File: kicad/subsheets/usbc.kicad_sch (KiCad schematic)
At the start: 15 parts

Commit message: Mark as R1.0
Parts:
- renumbered C5 to C6, C6 to C7, FB1 to FB2, FB2 to FB3, R46 to R17, R52 to R18
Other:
- company: (none) -> UVic Rocketry
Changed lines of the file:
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@@
 	(title_block
 		(title "USB C Port")
+		(date "2025-11-23")
+		(rev "1.0")
+		(company "UVic Rocketry")
+		(comment 1 "Author: Eric Handley")
 	)
 	(junction
@@
 		(on_board yes)
 		(dnp no)
-		(property "Reference" "#PWR093"
+		(property "Reference" "#PWR028"
 			(at 161.29 132.08 0)
 			(effects
@@
 			(project "srad-camera"
 				(path "/da62c771-e8c9-451f-8df1-ec995aadcb11/2d2335c5-b8ff-4d43-ae83-f45f6f125b07"
-					(reference "#PWR093")
+					(reference "#PWR028")
 					(unit 1)
 				)
@@
 		(on_board yes)
 		(dnp no)
-		(property "Reference" "FB1"
+		(property "Reference" "FB2"
 			(at 169.926 68.072 90)
 			(effects
@@
 			(project "srad-camera"
 				(path "/da62c771-e8c9-451f-8df1-ec995aadcb11/2d2335c5-b8ff-4d43-ae83-f45f6f125b07"
-					(reference "FB1")
+					(reference "FB2")
 					(unit 1)
 				)
@@
 		(on_board yes)
 		(dnp no)
-		(property "Reference" "#PWR019"
+		(property "Reference" "#PWR024"
 			(at 176.53 86.36 0)
 			(effects
@@
 			(project "srad-camera"
 				(path "/da62c771-e8c9-451f-8df1-ec995aadcb11/2d2335c5-b8ff-4d43-ae83-f45f6f125b07"
-					(reference "#PWR019")
+					(reference "#PWR024")
 					(unit 1)
 				)
@@
 		(dnp no)
 		(fields_autoplaced yes)
-		(property "Reference" "#PWR092"
+		(property "Reference" "#PWR026"
 			(at 156.21 116.84 0)
 			(effects
@@
 			(project "srad-camera"
 				(path "/da62c771-e8c9-451f-8df1-ec995aadcb11/2d2335c5-b8ff-4d43-ae83-f45f6f125b07"
-					(reference "#PWR092")
+					(reference "#PWR026")
 					(unit 1)
 				)
@@
 		(dnp no)
 		(fields_autoplaced yes)
-		(property "Reference" "C6"
+		(property "Reference" "C7"
 			(at 182.6641 72.4414 0)
 			(effects
@@
 			(project "srad-camera"
 				(path "/da62c771-e8c9-451f-8df1-ec995aadcb11/2d2335c5-b8ff-4d43-ae83-f45f6f125b07"
-					(reference "C6")
+					(reference "C7")
 					(unit 1)
 				)
@@
 		(on_board yes)
 		(dnp no)
-		(property "Reference" "FB2"
+		(property "Reference" "FB3"
 			(at 118.618 115.062 0)
 			(effects
@@
 			(project "srad-camera"
 				(path "/da62c771-e8c9-451f-8df1-ec995aadcb11/2d2335c5-b8ff-4d43-ae83-f45f6f125b07"
-					(reference "FB2")
+					(reference "FB3")
 					(unit 1)
 				)
@@
 		(dnp no)
 		(fields_autoplaced yes)
-		(property "Reference" "#PWR091"
+		(property "Reference" "#PWR021"
 			(at 167.64 64.77 0)
 			(effects
@@
 			(project "srad-camera"
 				(path "/da62c771-e8c9-451f-8df1-ec995aadcb11/2d2335c5-b8ff-4d43-ae83-f45f6f125b07"
-					(reference "#PWR091")
+					(reference "#PWR021")
 					(unit 1)
 				)
@@
 		(on_board yes)
 		(dnp no)
-		(property "Reference" "R52"
+		(property "Reference" "R18"
 			(at 162.56 121.158 0)
 			(effects
@@
 			(project "srad-camera"
 				(path "/da62c771-e8c9-451f-8df1-ec995aadcb11/2d2335c5-b8ff-4d43-ae83-f45f6f125b07"
-					(reference "R52")
+					(reference "R18")
 					(unit 1)
 				)
@@
 		(dnp no)
 		(fields_autoplaced yes)
-		(property "Reference" "C5"
+		(property "Reference" "C6"
 			(at 174.2059 72.4414 0)
 			(effects
@@
 			(project "srad-camera"
 				(path "/da62c771-e8c9-451f-8df1-ec995aadcb11/2d2335c5-b8ff-4d43-ae83-f45f6f125b07"
-					(reference "C5")
+					(reference "C6")
 					(unit 1)
 				)
@@
 		(dnp no)
 		(fields_autoplaced yes)
-		(property "Reference" "#PWR090"
+		(property "Reference" "#PWR022"
 			(at 134.62 73.66 0)
 			(effects
@@
 			(project ""
 				(path "/da62c771-e8c9-451f-8df1-ec995aadcb11/2d2335c5-b8ff-4d43-ae83-f45f6f125b07"
-					(reference "#PWR090")
+					(reference "#PWR022")
 					(unit 1)
 				)
@@
 		(on_board yes)
 		(dnp no)
-		(property "Reference" "#PWR020"
+		(property "Reference" "#PWR023"
 			(at 92.71 74.93 0)
 			(effects
@@
 			(project "srad-camera"
 				(path "/da62c771-e8c9-451f-8df1-ec995aadcb11/2d2335c5-b8ff-4d43-ae83-f45f6f125b07"
-					(reference "#PWR020")
+					(reference "#PWR023")
 					(unit 1)
 				)
@@
 		(on_board yes)
 		(dnp no)
-		(property "Reference" "R46"
+		(property "Reference" "R17"
 			(at 154.432 112.776 90)
 			(effects
@@
 			(project "srad-camera"
 				(path "/da62c771-e8c9-451f-8df1-ec995aadcb11/2d2335c5-b8ff-4d43-ae83-f45f6f125b07"
-					(reference "R46")
+					(reference "R17")
 					(unit 1)
 				)
@@
 		(dnp no)
 		(fields_autoplaced yes)
-		(property "Reference" "#PWR021"
+		(property "Reference" "#PWR025"
 			(at 140.97 111.76 0)
 			(effects
@@
 			(project "srad-camera"
 				(path "/da62c771-e8c9-451f-8df1-ec995aadcb11/2d2335c5-b8ff-4d43-ae83-f45f6f125b07"
-					(reference "#PWR021")
+					(reference "#PWR025")
 					(unit 1)
 				)
@@
 		(dnp no)
 		(fields_autoplaced yes)
-		(property "Reference" "#PWR022"
+		(property "Reference" "#PWR027"
 			(at 123.19 129.54 0)
 			(effects
@@
 			(project "srad-camera"
 				(path "/da62c771-e8c9-451f-8df1-ec995aadcb11/2d2335c5-b8ff-4d43-ae83-f45f6f125b07"
-					(reference "#PWR022")
+					(reference "#PWR027")
 					(unit 1)
 				)

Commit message: Start on PCB design
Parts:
- C6: footprint (none) -> Capacitor_SMD:C_0805_2012Metric; LCSC PART NAME (none) -> C15850
- C7: footprint (none) -> Capacitor_SMD:C_0402_1005Metric; LCSC PART NAME (none) -> C1525
- D2: value D_TVS <1uF -> TVS Vr3.3 Vb4; footprint (none) -> Diode_SMD:D_SOD-123F; LCSC PART NAME (none) -> C19077496
- D3: value TVS Vr3.3 Vb4 <1uF -> TVS Vr3.3 Vb4; footprint (none) -> Diode_SMD:D_SOD-123F; LCSC PART NAME (none) -> C19077496
- FB2, FB3: value FerriteBead_Small -> 120R; footprint (none) -> Resistor_SMD:R_0201_0603Metric; LCSC PART NAME (none) -> C14709
- R14: renamed from R12; footprint (none) -> Resistor_SMD:R_0402_1005Metric; LCSC PART NAME (none) -> C25905
- R15: renamed from R13; footprint (none) -> Resistor_SMD:R_0402_1005Metric; LCSC PART NAME (none) -> C25905
- R16: renamed from R14; value 2.2R -> 22R; footprint (none) -> Resistor_SMD:R_0402_1005Metric; LCSC PART NAME (none) -> C25092
- R17: renamed from R15; value 2.2R -> 22R; footprint (none) -> Resistor_SMD:R_0402_1005Metric; LCSC PART NAME (none) -> C25092
- R18: renamed from R16; footprint (none) -> Resistor_SMD:R_0402_1005Metric; LCSC PART NAME (none) -> C26083
- R19: renamed from R17; footprint (none) -> Resistor_SMD:R_0402_1005Metric; LCSC PART NAME (none) -> C25744
- R20: renamed from R18; value 15k -> 10k; footprint (none) -> Resistor_SMD:R_0402_1005Metric; LCSC PART NAME (none) -> C25744
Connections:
- net USB_DM renamed USB_DN
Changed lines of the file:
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@@
 		)
 	)
-	(hierarchical_label "USB_DM"
+	(hierarchical_label "USB_DN"
 		(shape output)
 		(at 156.21 87.63 0)
@@
 			)
 		)
-		(property "Value" "FerriteBead_Small"
+		(property "Value" "120R"
 			(at 168.148 68.58 90)
 			(effects
@@
 			)
 		)
-		(property "Footprint" ""
+		(property "Footprint" "Resistor_SMD:R_0201_0603Metric"
 			(at 171.45 66.548 90)
 			(effects
@@
 		)
 		(property "SUPPLEMENTARY FEATURES" ""
+			(at 171.45 64.77 90)
+			(effects
+				(font
+					(size 1.27 1.27)
+				)
+				(hide yes)
+			)
+		)
+		(property "LCSC PART NAME" "C14709"
 			(at 171.45 64.77 90)
 			(effects
@@
 		(dnp no)
 		(fields_autoplaced yes)
-		(property "Reference" "R14"
+		(property "Reference" "R16"
 			(at 148.59 82.9533 90)
 			(effects
@@
 			)
 		)
-		(property "Value" "2.2R"
+		(property "Value" "22R"
 			(at 148.59 85.1732 90)
 			(effects
@@
 			)
 		)
-		(property "Footprint" ""
+		(property "Footprint" "Resistor_SMD:R_0402_1005Metric"
 			(at 148.59 87.63 0)
 			(effects
@@
 		)
 		(property "SUPPLEMENTARY FEATURES" ""
+			(at 148.59 87.63 90)
+			(effects
+				(font
+					(size 1.27 1.27)
+				)
+				(hide yes)
+			)
+		)
+		(property "LCSC PART NAME" "C25092"
 			(at 148.59 87.63 90)
 			(effects
@@
 			(project "srad-camera"
 				(path "/da62c771-e8c9-451f-8df1-ec995aadcb11/2d2335c5-b8ff-4d43-ae83-f45f6f125b07"
-					(reference "R14")
+					(reference "R16")
 					(unit 1)
 				)
@@
 			)
 		)
-		(property "Footprint" ""
+		(property "Footprint" "Capacitor_SMD:C_0402_1005Metric"
 			(at 180.34 73.66 0)
 			(effects
@@
 			)
 		)
-		(property "V" ""
+		(property "LCSC PART NAME" "C1525"
 			(at 180.34 73.66 0)
 			(effects
@@
 			)
 		)
-		(property "Value" "TVS Vr3.3 Vb4 <1uF"
+		(property "Value" "TVS Vr3.3 Vb4"
 			(at 146.304 102.3621 90)
 			(effects
@@
 			)
 		)
-		(property "Footprint" ""
+		(property "Footprint" "Diode_SMD:D_SOD-123F"
 			(at 144.78 100.33 0)
 			(effects
@@
 		)
 		(property "SUPPLEMENTARY FEATURES" ""
+			(at 144.78 100.33 90)
+			(effects
+				(font
+					(size 1.27 1.27)
+				)
+				(hide yes)
+			)
+		)
+		(property "LCSC PART NAME" "C19077496"
 			(at 144.78 100.33 90)
 			(effects
@@
 			)
 		)
-		(property "Value" "FerriteBead_Small"
+		(property "Value" "120R"
 			(at 119.126 113.284 0)
 			(effects
@@
 			)
 		)
-		(property "Footprint" ""
+		(property "Footprint" "Resistor_SMD:R_0201_0603Metric"
 			(at 116.332 116.84 90)
 			(effects
@@
 		)
 		(property "SUPPLEMENTARY FEATURES" ""
+			(at 118.11 116.84 0)
+			(effects
+				(font
+					(size 1.27 1.27)
+				)
+				(hide yes)
+			)
+		)
+		(property "LCSC PART NAME" "C14709"
 			(at 118.11 116.84 0)
 			(effects
@@
 		(on_board yes)
 		(dnp no)
-		(property "Reference" "R18"
+		(property "Reference" "R20"
 			(at 162.56 121.158 0)
 			(effects
@@
 			)
 		)
-		(property "Value" "15k"
+		(property "Value" "10k"
 			(at 162.56 122.936 0)
 			(effects
@@
 			)
 		)
-		(property "Footprint" ""
+		(property "Footprint" "Resistor_SMD:R_0402_1005Metric"
 			(at 161.29 121.92 0)
 			(effects
@@
 		)
 		(property "SUPPLEMENTARY FEATURES" ""
+			(at 161.29 121.92 0)
+			(effects
+				(font
+					(size 1.27 1.27)
+				)
+				(hide yes)
+			)
+		)
+		(property "LCSC PART NAME" "C25744"
 			(at 161.29 121.92 0)
 			(effects
@@
 			(project "srad-camera"
 				(path "/da62c771-e8c9-451f-8df1-ec995aadcb11/2d2335c5-b8ff-4d43-ae83-f45f6f125b07"
-					(reference "R18")
+					(reference "R20")
 					(unit 1)
 				)
@@
 			)
 		)
-		(property "Footprint" ""
+		(property "Footprint" "Capacitor_SMD:C_0805_2012Metric"
 			(at 176.53 73.66 0)
 			(effects
@@
 		)
 		(property "SUPPLEMENTARY FEATURES" ""
+			(at 176.53 73.66 0)
+			(effects
+				(font
+					(size 1.27 1.27)
+				)
+				(hide yes)
+			)
+		)
+		(property "LCSC PART NAME" "C15850"
 			(at 176.53 73.66 0)
 			(effects
@@
 			)
 		)
-		(property "Value" "D_TVS <1uF"
+		(property "Value" "TVS Vr3.3 Vb4"
 			(at 143.51 101.5999 90)
 			(effects
@@
 			)
 		)
-		(property "Footprint" ""
+		(property "Footprint" "Diode_SMD:D_SOD-123F"
 			(at 140.97 100.33 0)
 			(effects
@@
 		)
 		(property "SUPPLEMENTARY FEATURES" ""
+			(at 140.97 100.33 90)
+			(effects
+				(font
+					(size 1.27 1.27)
+				)
+				(hide yes)
+			)
+		)
+		(property "LCSC PART NAME" "C19077496"
 			(at 140.97 100.33 90)
 			(effects
@@
 		(dnp no)
 		(fields_autoplaced yes)
-		(property "Reference" "R12"
+		(property "Reference" "R14"
 			(at 104.14 68.9833 90)
 			(effects
@@
 			)
 		)
-		(property "Footprint" ""
+		(property "Footprint" "Resistor_SMD:R_0402_1005Metric"
 			(at 104.14 73.66 0)
 			(effects
@@
 		)
 		(property "SUPPLEMENTARY FEATURES" ""
+			(at 104.14 73.66 90)
+			(effects
+				(font
+					(size 1.27 1.27)
+				)
+				(hide yes)
+			)
+		)
+		(property "LCSC PART NAME" "C25905"
 			(at 104.14 73.66 90)
 			(effects
@@
 			(project "srad-camera"
 				(path "/da62c771-e8c9-451f-8df1-ec995aadcb11/2d2335c5-b8ff-4d43-ae83-f45f6f125b07"
-					(reference "R12")
+					(reference "R14")
 					(unit 1)
 				)
@@
 		(on_board yes)
 		(dnp no)
-		(property "Reference" "R17"
+		(property "Reference" "R19"
 			(at 154.432 112.776 90)
 			(effects
@@
 			)
 		)
-		(property "Footprint" ""
+		(property "Footprint" "Resistor_SMD:R_0402_1005Metric"
 			(at 156.21 116.84 0)
 			(effects
@@
 		(property "SUPPLEMENTARY FEATURES" ""
 			(at 156.21 116.84 0)
+			(effects
+				(font
+					(size 1.27 1.27)
+				)
+				(hide yes)
+			)
+		)
+		(property "LCSC PART NAME" "C25744"
+			(at 156.21 116.84 90)
 			(effects
 				(font
@@
 			(project "srad-camera"
 				(path "/da62c771-e8c9-451f-8df1-ec995aadcb11/2d2335c5-b8ff-4d43-ae83-f45f6f125b07"
-					(reference "R17")
+					(reference "R19")
 					(unit 1)
 				)
@@
 		(on_board yes)
 		(dnp no)
-		(property "Reference" "R16"
+		(property "Reference" "R18"
 			(at 111.252 116.078 0)
 			(effects
@@
 			)
 		)
-		(property "Footprint" ""
+		(property "Footprint" "Resistor_SMD:R_0402_1005Metric"
 			(at 113.03 116.84 0)
 			(effects
@@
 		)
 		(property "SUPPLEMENTARY FEATURES" ""
+			(at 113.03 116.84 0)
+			(effects
+				(font
+					(size 1.27 1.27)
+				)
+				(hide yes)
+			)
+		)
+		(property "LCSC PART NAME" "C26083"
 			(at 113.03 116.84 0)
 			(effects
@@
 			(project "srad-camera"
 				(path "/da62c771-e8c9-451f-8df1-ec995aadcb11/2d2335c5-b8ff-4d43-ae83-f45f6f125b07"
-					(reference "R16")
+					(reference "R18")
 					(unit 1)
 				)
@@
 		(dnp no)
 		(fields_autoplaced yes)
-		(property "Reference" "R15"
+		(property "Reference" "R17"
 			(at 148.59 94.9623 90)
 			(effects
@@
 			)
 		)
-		(property "Value" "2.2R"
+		(property "Value" "22R"
 			(at 148.59 97.1822 90)
 			(effects
@@
 			)
 		)
-		(property "Footprint" ""
+		(property "Footprint" "Resistor_SMD:R_0402_1005Metric"
 			(at 148.59 92.71 0)
 			(effects
@@
 		)
 		(property "SUPPLEMENTARY FEATURES" ""
+			(at 148.59 92.71 90)
+			(effects
+				(font
+					(size 1.27 1.27)
+				)
+				(hide yes)
+			)
+		)
+		(property "LCSC PART NAME" "C25092"
 			(at 148.59 92.71 90)
 			(effects
@@
 			(project "srad-camera"
 				(path "/da62c771-e8c9-451f-8df1-ec995aadcb11/2d2335c5-b8ff-4d43-ae83-f45f6f125b07"
-					(reference "R15")
+					(reference "R17")
 					(unit 1)
 				)
@@
 		(dnp no)
 		(fields_autoplaced yes)
-		(property "Reference" "R13"
+		(property "Reference" "R15"
 			(at 104.14 78.4523 90)
 			(effects
@@
 			)
 		)
-		(property "Footprint" ""
+		(property "Footprint" "Resistor_SMD:R_0402_1005Metric"
 			(at 104.14 76.2 0)
 			(effects
@@
 		)
 		(property "SUPPLEMENTARY FEATURES" ""
+			(at 104.14 76.2 90)
+			(effects
+				(font
+					(size 1.27 1.27)
+				)
+				(hide yes)
+			)
+		)
+		(property "LCSC PART NAME" "C25905"
 			(at 104.14 76.2 90)
 			(effects
@@
 			(project "srad-camera"
 				(path "/da62c771-e8c9-451f-8df1-ec995aadcb11/2d2335c5-b8ff-4d43-ae83-f45f6f125b07"
-					(reference "R13")
+					(reference "R15")
 					(unit 1)
 				)

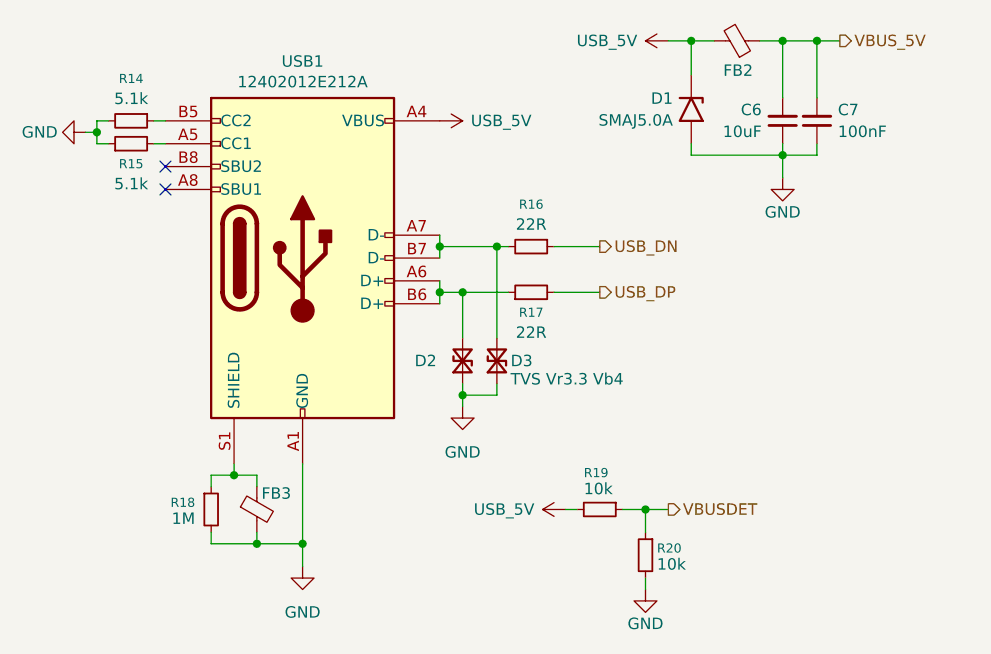
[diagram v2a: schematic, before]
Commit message: Remove power/decoupling for unused power domains
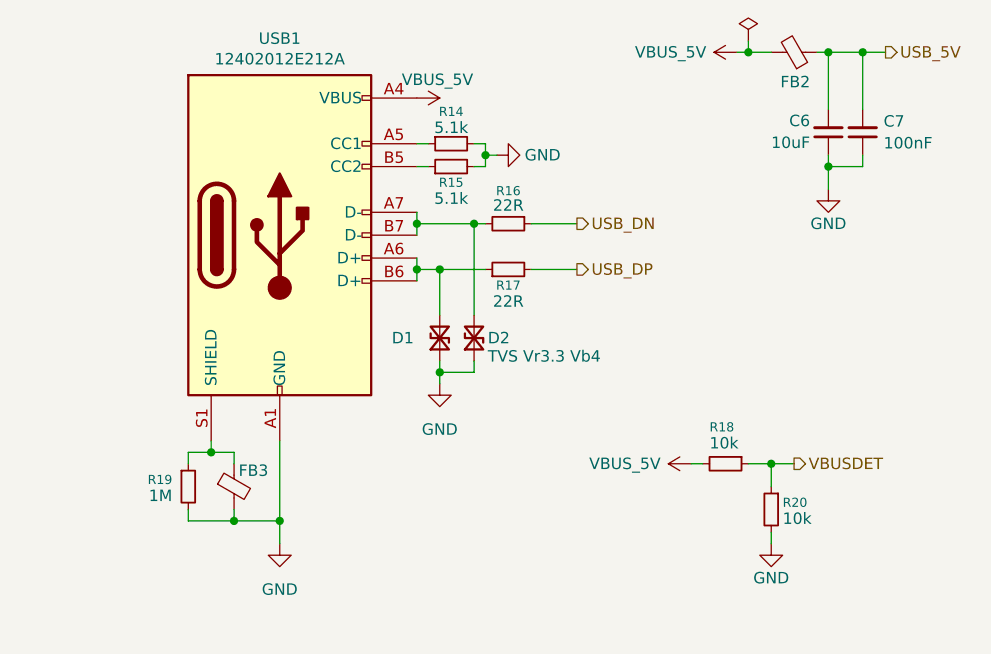
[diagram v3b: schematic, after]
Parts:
- removed D1: SMAJ5.0A, Diode_SMD:D_SMA, symbol Diode:SMAJ5.0A
- USB1: footprint srad-camera-footprints:USB-SMD_TYPE-C16PIN-1 -> Connector_USB:USB_C_Receptacle_G-Switch_GT-USB-7010ASV; symbol Connector:USB_C_Receptacle_USB2.0_16P -> Connector:USB_C_Receptacle_USB2.0_14P
- renumbered D2 to D1, D3 to D2, R19 to R18, R18 to R19
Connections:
- net GND: now also R15.2; no longer R15.1
- net USB_5V: now also C6.2, C7.2, FB2.1; no longer FB2.2, R18.2, USB1.A4 (VBUS), USB1.A9 (VBUS), USB1.B4 (VBUS), USB1.B9 (VBUS)
- net VBUS_5V: now also FB2.2, R18.2, USB1.A4 (VBUS), USB1.A9 (VBUS), USB1.B4 (VBUS), USB1.B9 (VBUS); no longer C6.2, C7.2, FB2.1
- net at USB1.A5 (CC1): now also R14.1; no longer R15.2
- net at USB1.B5 (CC2): now also R15.1; no longer R14.1
- no-connect marks 2 -> 0
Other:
- moved on the sheet: C6, C7, D1, D2, FB2, FB3, R14, R16, R17, R18, R19, R20

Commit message: All major components placed on board
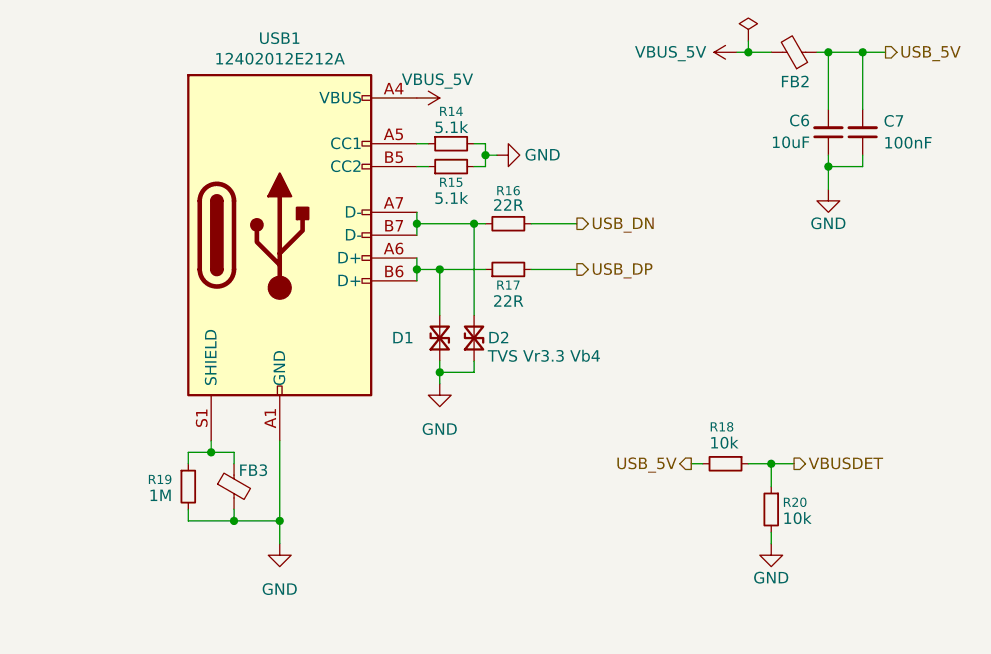
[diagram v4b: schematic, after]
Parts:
- USB1: footprint Connector_USB:USB_C_Receptacle_G-Switch_GT-USB-7010ASV -> Connector_USB:USB_C_Receptacle_HRO_TYPE-C-31-M-12
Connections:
- net USB_5V: now also R18.2
- net VBUS_5V: no longer R18.2
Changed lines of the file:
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@@
+		)
+	)
+	(hierarchical_label "USB_5V"
+		(shape output)
+		(at 166.37 111.76 180)
+		(effects
+			(font
+				(size 1.27 1.27)
+			)
+			(justify right)
 		)
 	)
@@
 				(path "/da62c771-e8c9-451f-8df1-ec995aadcb11/2d2335c5-b8ff-4d43-ae83-f45f6f125b07"
 					(reference "#PWR028")
-					(unit 1)
-				)
-			)
-		)
-	)
-	(symbol
-		(lib_id "power:VCC")
-		(at 166.37 111.76 90)
-		(unit 1)
-		(exclude_from_sim no)
-		(in_bom yes)
-		(on_board yes)
-		(dnp no)
-		(fields_autoplaced yes)
-		(property "Reference" "#PWR030"
-			(at 170.18 111.76 0)
-			(effects
-				(font
-					(size 1.27 1.27)
-				)
-				(hide yes)
-			)
-		)
-		(property "Value" "VBUS_5V"
-			(at 159.0017 111.76 90)
-			(effects
-				(font
-					(size 1.27 1.27)
-				)
-			)
-		)
-		(property "Footprint" ""
-			(at 166.37 111.76 0)
-			(effects
-				(font
-					(size 1.27 1.27)
-				)
-				(hide yes)
-			)
-		)
-		(property "Datasheet" ""
-			(at 166.37 111.76 0)
-			(effects
-				(font
-					(size 1.27 1.27)
-				)
-				(hide yes)
-			)
-		)
-		(property "Description" "Power symbol creates a global label with name \"VCC\""
-			(at 166.37 111.76 0)
-			(effects
-				(font
-					(size 1.27 1.27)
-				)
-				(hide yes)
-			)
-		)
-		(pin "1"
-		)
-		(instances
-			(project "srad-camera"
-				(path "/da62c771-e8c9-451f-8df1-ec995aadcb11/2d2335c5-b8ff-4d43-ae83-f45f6f125b07"
-					(reference "#PWR030")
 					(unit 1)
 				)
@@
 			)
 		)
-		(property "Footprint" "Connector_USB:USB_C_Receptacle_G-Switch_GT-USB-7010ASV"
+		(property "Footprint" "Connector_USB:USB_C_Receptacle_HRO_TYPE-C-31-M-12"
 			(at 124.46 86.36 0)
 			(effects
